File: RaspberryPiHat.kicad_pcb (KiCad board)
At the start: 2 copper layers, 9 parts, among them J1 Raspberry_Pi_2_3, SW1 SW_DPST, U1 DHT22

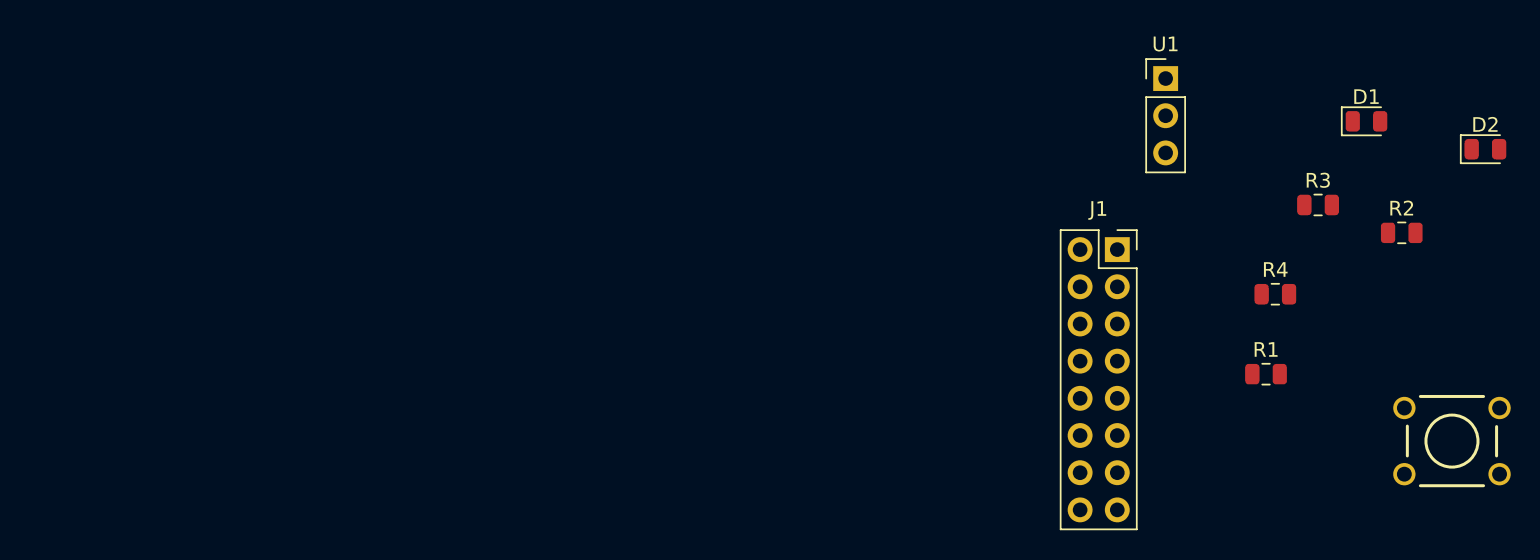
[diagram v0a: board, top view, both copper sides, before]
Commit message: PCB board with components place - no rounded edges
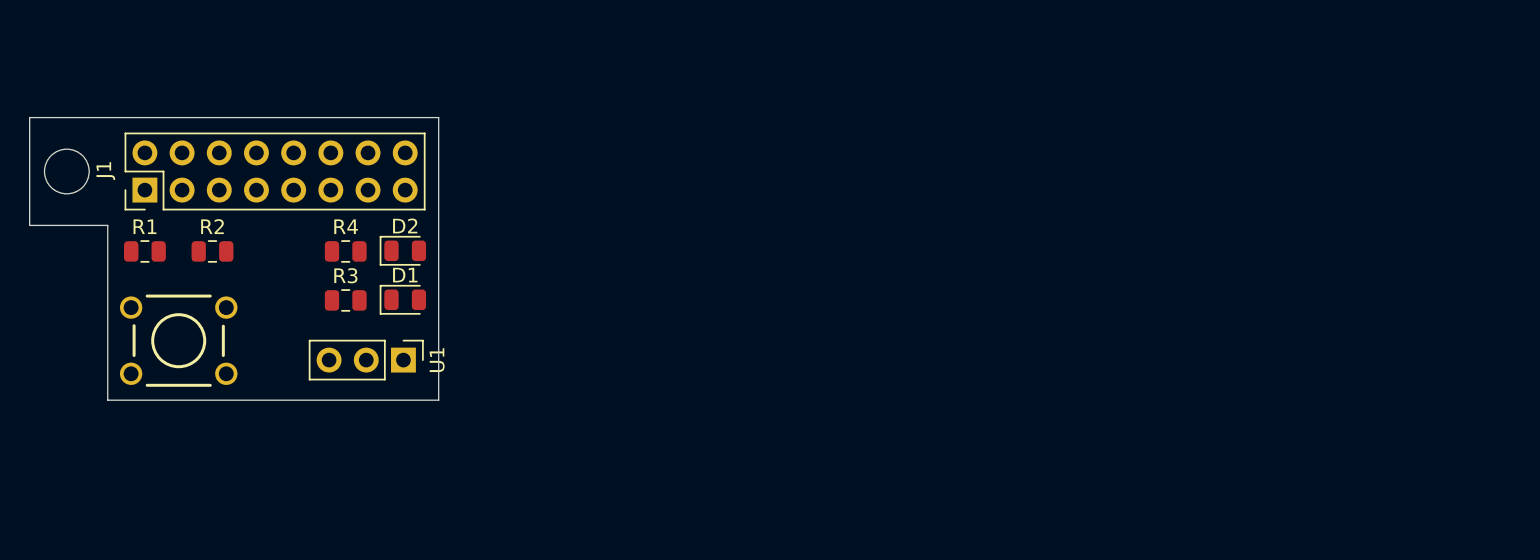
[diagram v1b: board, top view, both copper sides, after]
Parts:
- J1: footprint Connector_PinSocket_2.54mm:PinSocket_2x08_P2.54mm_Vertical -> Connector_PinHeader_2.54mm:PinHeader_2x08_P2.54mm_Vertical
- moved SW1 87.2 mm to (94.8, 79.0)
- moved R2 81.2 mm to (97.1, 72.9)
- moved R1 77.0 mm to (92.5, 72.9)
- moved D2 74.1 mm to (110.2, 72.9)
- moved D1 66.8 mm to (110.2, 76.2)
- moved R3 66.7 mm to (106.2, 76.2)
- moved J1 66.5 mm to (92.5, 68.7), turned to 90 degrees
- moved R4 63.6 mm to (106.2, 72.9)
- moved U1 55.5 mm to (110.1, 80.3), turned to 270 degrees
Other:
- board outline added: 27.9 x 19.3 mm
